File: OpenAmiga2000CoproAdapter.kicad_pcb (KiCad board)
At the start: 2 copper layers, 112 x 37.5 mm, 7 parts, among them CN1 A2000_COPRO_SLOT, P1 CONN_2, P2 CONN_2, P3 CONN_2, P4 CONN_2, P99 OSHW_LOGO, U1 68000D

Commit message: Add silkscreen hint for the FCx lines
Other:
- board text added: "FC2/1/0"
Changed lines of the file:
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@@
   (general
     (thickness 1.6)
-    (drawings 19)
+    (drawings 20)
     (tracks 338)
     (zones 0)
@@
   (title_block
     (title OpenAmiga2000CoproAdapter)
-    (date 2018-10-28)
+    (date 2018-10-29)
     (rev 1git)
     (company SukkoPera)
@@
     (0 F.Cu signal)
     (31 B.Cu signal)
-    (36 B.SilkS user hide)
-    (37 F.SilkS user hide)
-    (38 B.Mask user hide)
-    (39 F.Mask user hide)
+    (36 B.SilkS user)
+    (37 F.SilkS user)
+    (38 B.Mask user)
+    (39 F.Mask user)
     (44 Edge.Cuts user)
     (45 Margin user hide)
     (46 B.CrtYd user hide)
-    (47 F.CrtYd user)
+    (47 F.CrtYd user hide)
     (49 F.Fab user hide)
   )
@@
       (xy 0.500964 3.601424)) (layer B.Cu) (width 0.01))
   )
+  (gr_text FC2/1/0 (at 141.478 116.332) (layer B.SilkS)
+    (effects (font (size 1 1) (thickness 0.15)) (justify mirror))
+  )
   (gr_line (start 99.06 116.84) (end 100.33 115.57) (layer F.SilkS) (width 0.3))

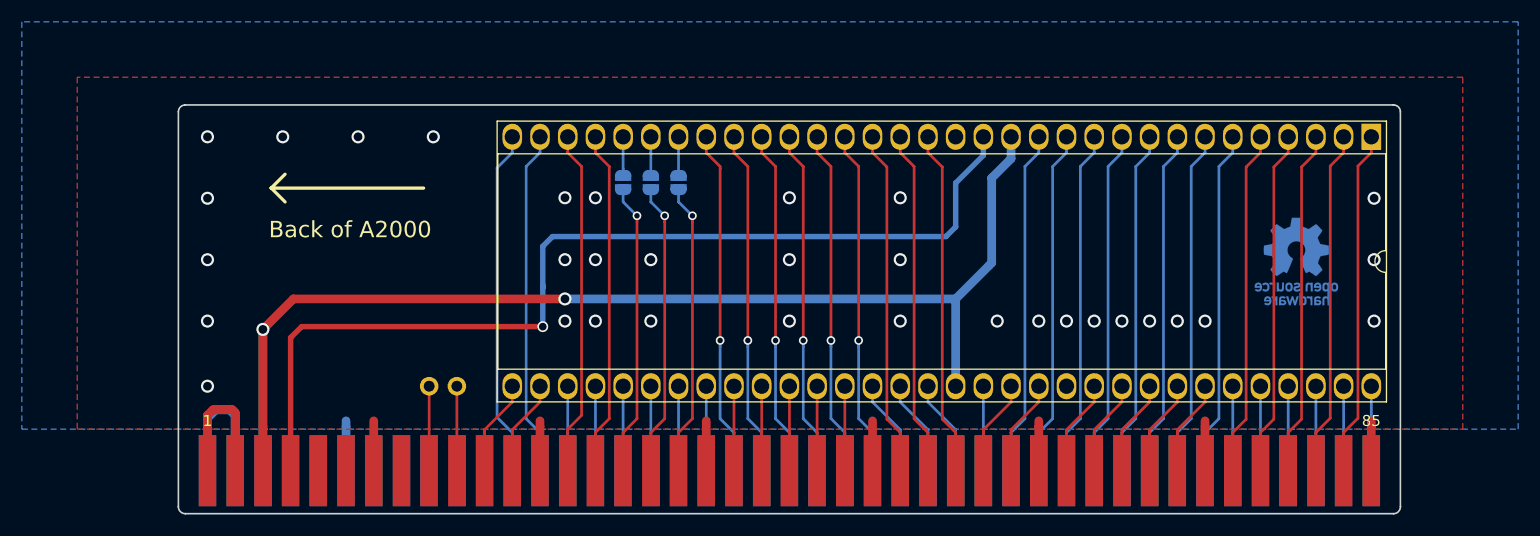
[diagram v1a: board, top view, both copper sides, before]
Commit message: Nicer placement of +5V/Clock traces
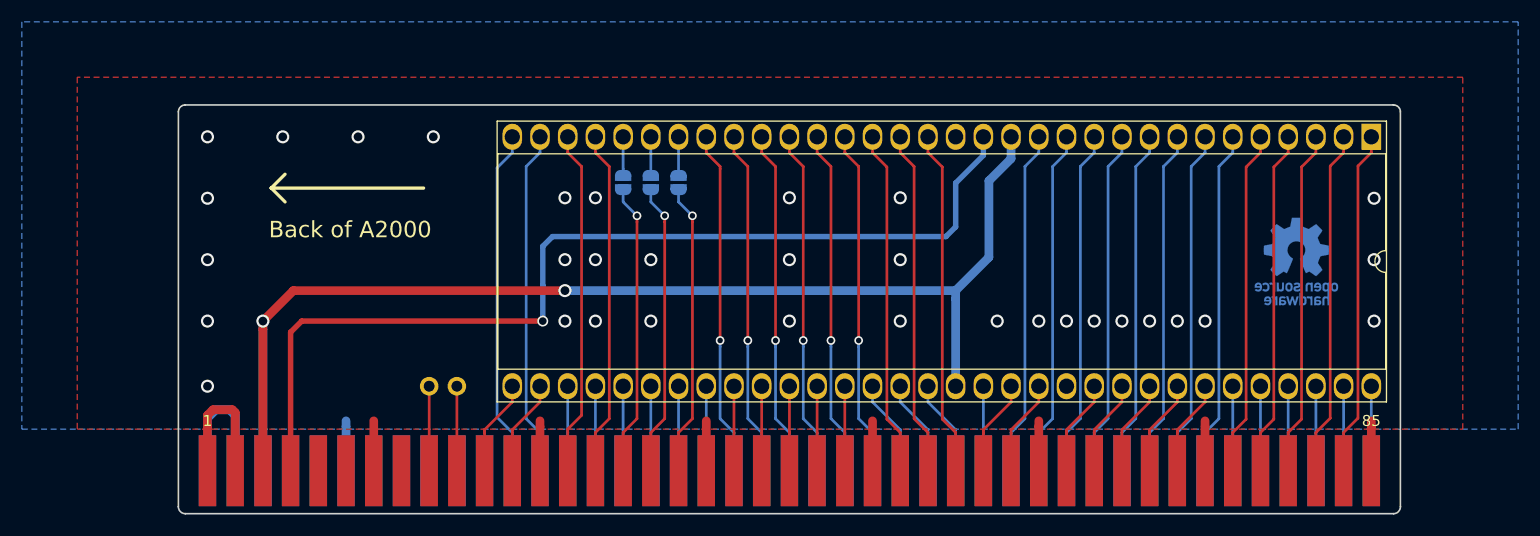
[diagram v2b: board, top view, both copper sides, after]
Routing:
- net +5V: track 115.5 -> 117.1 mm
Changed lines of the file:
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@@
     (thickness 1.6)
     (drawings 20)
-    (tracks 338)
+    (tracks 339)
     (zones 0)
     (modules 7)
@@
   (title_block
     (title OpenAmiga2000CoproAdapter)
-    (date 2018-10-29)
+    (date 2018-10-30)
     (rev 1git)
     (company SukkoPera)
@@
   (via (at 133.858 123.401666) (size 1.2) (drill 0.8) (layers F.Cu B.Cu) (net 1))
   (via (at 93.218 135.001) (size 1.2) (drill 0.8) (layers F.Cu B.Cu) (net 1))
-  (segment (start 98.298 142.748) (end 98.298 138.698) (width 0.8) (layer F.Cu) (net 2))
-  (segment (start 98.298 138.698) (end 98.298 129.794) (width 0.8) (layer F.Cu) (net 2))
-  (via (at 125.984 127) (size 1.2) (drill 0.8) (layers F.Cu B.Cu) (net 2))
-  (segment (start 98.298 129.794) (end 101.092 127) (width 0.8) (layer F.Cu) (net 2))
-  (segment (start 101.092 127) (end 125.984 127) (width 0.8) (layer F.Cu) (net 2))
-  (segment (start 125.984 127) (end 161.798 127) (width 0.8) (layer B.Cu) (net 2))
+  (via (at 125.984 126.238) (size 1.2) (drill 0.8) (layers F.Cu B.Cu) (net 2))
+  (segment (start 101.092 126.238) (end 125.984 126.238) (width 0.8) (layer F.Cu) (net 2))
+  (segment (start 125.984 126.238) (end 161.798 126.238) (width 0.8) (layer B.Cu) (net 2))
   (segment (start 161.798 135.001) (end 161.798 127) (width 0.8) (layer B.Cu) (net 2))
-  (via (at 98.298 129.794) (size 1.2) (drill 0.8) (layers F.Cu B.Cu) (net 2))
   (segment (start 98.298 142.748) (end 98.298 129.794) (width 0.8) (layer B.Cu) (net 2))
-  (segment (start 164.846 123.952) (end 161.798 127) (width 0.8) (layer B.Cu) (net 2))
-  (segment (start 165.1 123.698) (end 164.846 123.952) (width 0.8) (layer B.Cu) (net 2))
-  (segment (start 166.878 114.141) (end 165.1 115.919) (width 0.8) (layer B.Cu) (net 2))
-  (segment (start 166.878 112.141) (end 166.878 114.141) (width 0.8) (layer B.Cu) (net 2))
-  (segment (start 165.1 115.919) (end 165.1 123.698) (width 0.8) (layer B.Cu) (net 2))
-  (via (at 123.952 129.54) (size 1) (drill 0.7) (layers F.Cu B.Cu) (net 3))
+  (segment (start 161.798 127) (end 161.798 126.238) (width 0.8) (layer B.Cu) (net 2))
+  (segment (start 166.878 114.141) (end 166.878 112.141) (width 0.8) (layer B.Cu) (net 2))
+  (segment (start 164.846 116.173) (end 166.878 114.141) (width 0.8) (layer B.Cu) (net 2))
+  (segment (start 161.798 126.238) (end 164.846 123.19) (width 0.8) (layer B.Cu) (net 2))
+  (segment (start 164.846 123.19) (end 164.846 116.173) (width 0.8) (layer B.Cu) (net 2))
+  (via (at 98.298 129.032) (size 1.2) (drill 0.8) (layers F.Cu B.Cu) (net 2))
+  (segment (start 98.298 129.794) (end 98.298 129.032) (width 0.8) (layer B.Cu) (net 2))
+  (segment (start 98.298 129.794) (end 98.298 129.032) (width 0.8) (layer F.Cu) (net 2))
+  (segment (start 98.298 142.748) (end 98.298 129.794) (width 0.8) (layer F.Cu) (net 2))
+  (segment (start 101.092 126.238) (end 98.298 129.032) (width 0.8) (layer F.Cu) (net 2))
+  (via (at 123.952 129.032) (size 1) (drill 0.7) (layers F.Cu B.Cu) (net 3))
   (segment (start 123.952 125.73) (end 123.952 125.984) (width 0.5) (layer B.Cu) (net 3))
-  (segment (start 123.952 125.984) (end 123.952 129.54) (width 0.5) (layer B.Cu) (net 3))
-  (segment (start 101.854 129.54) (end 100.838 130.556) (width 0.5) (layer F.Cu) (net 3))
-  (segment (start 100.838 130.556) (end 100.838 142.748) (width 0.5) (layer F.Cu) (net 3))
-  (segment (start 123.952 129.54) (end 101.854 129.54) (width 0.5) (layer F.Cu) (net 3))
   (segment (start 164.338 113.841) (end 164.338 112.141) (width 0.5) (layer B.Cu) (net 3))
   (segment (start 123.952 125.984) (end 123.952 122.174) (width 0.5) (layer B.Cu) (net 3))
@@
   (segment (start 161.798 120.396) (end 161.798 116.381) (width 0.5) (layer B.Cu) (net 3))
   (segment (start 161.798 116.381) (end 164.338 113.841) (width 0.5) (layer B.Cu) (net 3))
+  (segment (start 123.952 125.984) (end 123.952 129.032) (width 0.5) (layer B.Cu) (net 3))
+  (segment (start 101.854 129.032) (end 123.952 129.032) (width 0.5) (layer F.Cu) (net 3))
+  (segment (start 100.838 142.748) (end 100.838 130.048) (width 0.5) (layer F.Cu) (net 3))
+  (segment (start 100.838 130.048) (end 101.854 129.032) (width 0.5) (layer F.Cu) (net 3))
   (segment (start 113.538 135.001) (end 113.538 142.748) (width 0.25) (layer F.Cu) (net 4))
   (segment (start 116.078 135.001) (end 116.078 142.748) (width 0.25) (layer F.Cu) (net 5))
